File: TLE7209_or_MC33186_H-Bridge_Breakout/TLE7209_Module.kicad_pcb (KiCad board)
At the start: 2 copper layers, 43 x 22 mm, 12 parts, among them J1 Conn_02x06_Odd_Even, J3 Conn_01x01, U1 TLE7209-2R

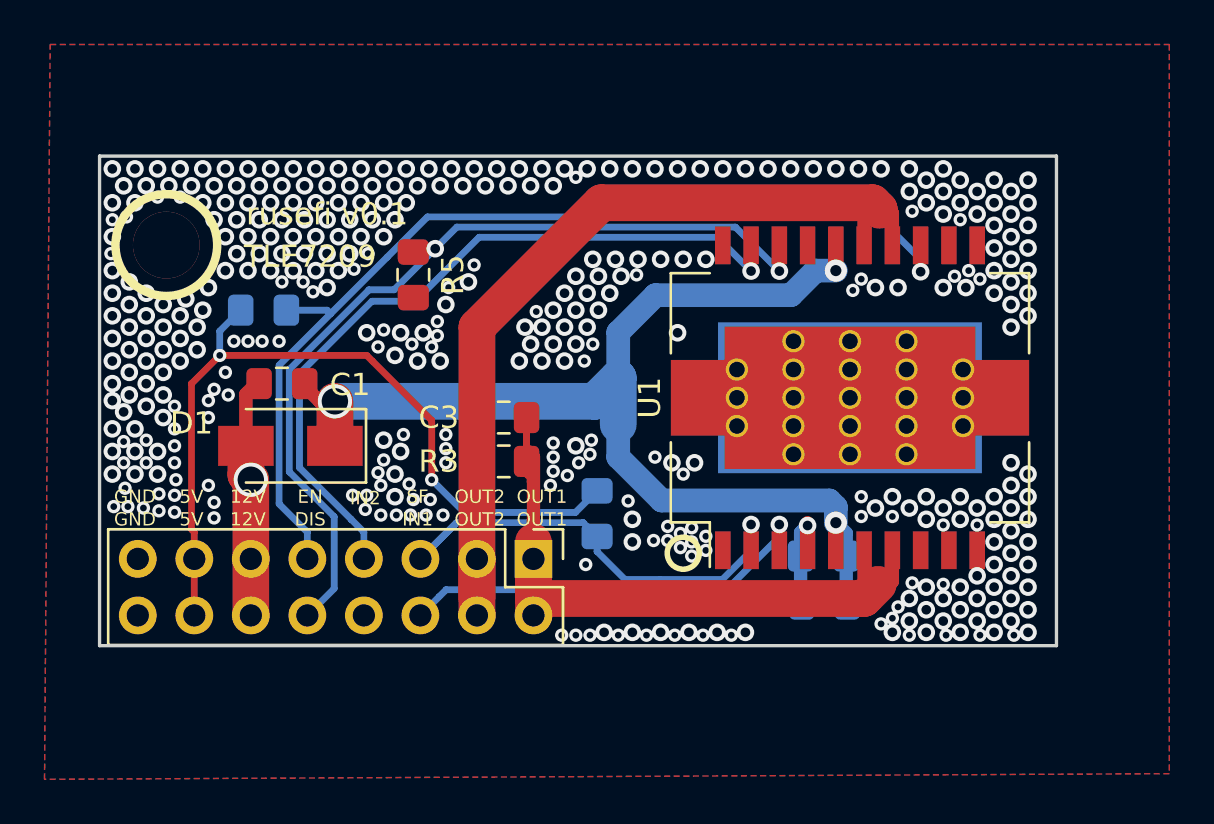
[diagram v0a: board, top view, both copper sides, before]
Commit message: Corrected schematic with LSLC Parts numbers (#25)
* Small update

* Updated with LSLC Pn

* pdf

* Pcb Update

* Gerbers

* larger cap
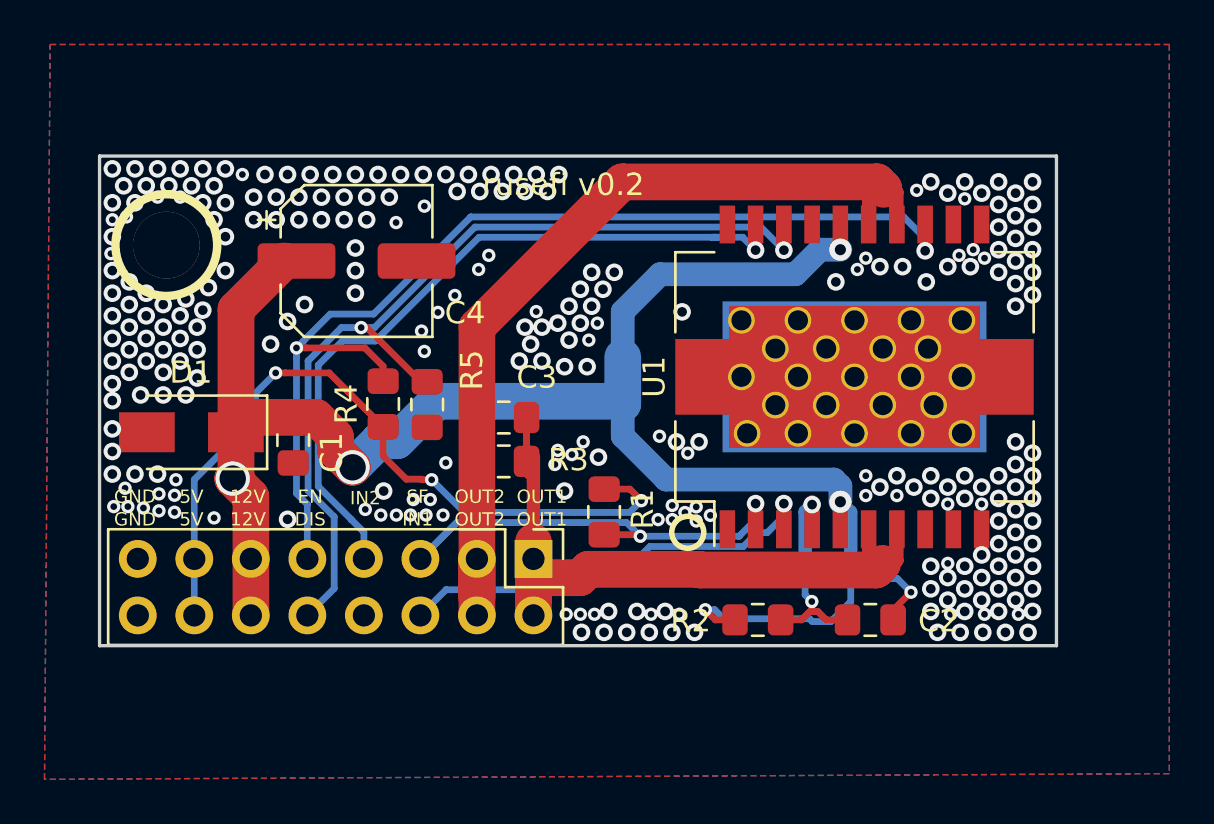
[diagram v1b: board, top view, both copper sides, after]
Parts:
- added C4: CP1, Capacitor_SMD:CP_Elec_6.3x5.7, F.Cu at (31.5, 24.7)
- C2, R1, R2, R4: moved to F.Cu
- moved R4 6.83 mm to (32.7, 31.1), turned to 270 degrees
- moved R5 5.86 mm to (34.7, 31.2)
- moved D1 4.49 mm to (24.1, 32.4)
- moved C2 3.56 mm to (54.6, 40.8)
- moved R2 3.08 mm to (49.6, 40.8), turned to 0 degrees
- moved C1 2.59 mm to (28.7, 32.8), turned to 270 degrees
- moved U1 0.96 mm to (53.9, 29.9)
- moved R1 0.33 mm to (42.7, 36.0)
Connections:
- C1 pad 1: Net-(C1-Pad1) -> /12V
- C1 pad 2: /12V -> GND
- C2 pad 1: Net-(C1-Pad1) -> /12V
- D1 pad 1: Net-(C1-Pad1) -> /12V
- D1 pad 2: /12V -> GND
- R2 pad 1: Net-(C1-Pad1) -> /12V
- U1 pad 16: Net-(C1-Pad1) -> /12V
- U1 pad 5: Net-(C1-Pad1) -> /12V
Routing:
- net /12V: track 10.8 -> 85.7 mm, vias 1 -> 6
- net Net-(C1-Pad1): track 51.0 -> 0.00 mm, vias 3 -> 0
- net Net-(C2-Pad2): track 4.69 -> 9.51 mm, vias 1 -> 2
- net /5V: track 36.5 -> 34.3 mm, vias 2 -> 3
- net /EN: track 45.4 -> 47.4 mm, vias 1 -> 2
- net /DIS: track 40.1 -> 41.3 mm
- net /IN2: track 34.1 -> 33.2 mm
- net /IN1: track 19.5 -> 20.0 mm
- net /OUT2: track 39.6 -> 40.2 mm
- net /SF: vias 1 -> 2
- net GND: vias 391 -> 271
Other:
- board text added: "rusefi v0.2"
- board text removed: "TLE7209"
- board text removed: "rusefi v0.1"
